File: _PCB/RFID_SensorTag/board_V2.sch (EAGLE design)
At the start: 21 parts, among them J2 SMT, J3 SMT, M2 BATTERY-CHARGER-LI-PROT, U1 MAXIM_ELECTRONICS_MAX40200AUK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, X1 53048-02

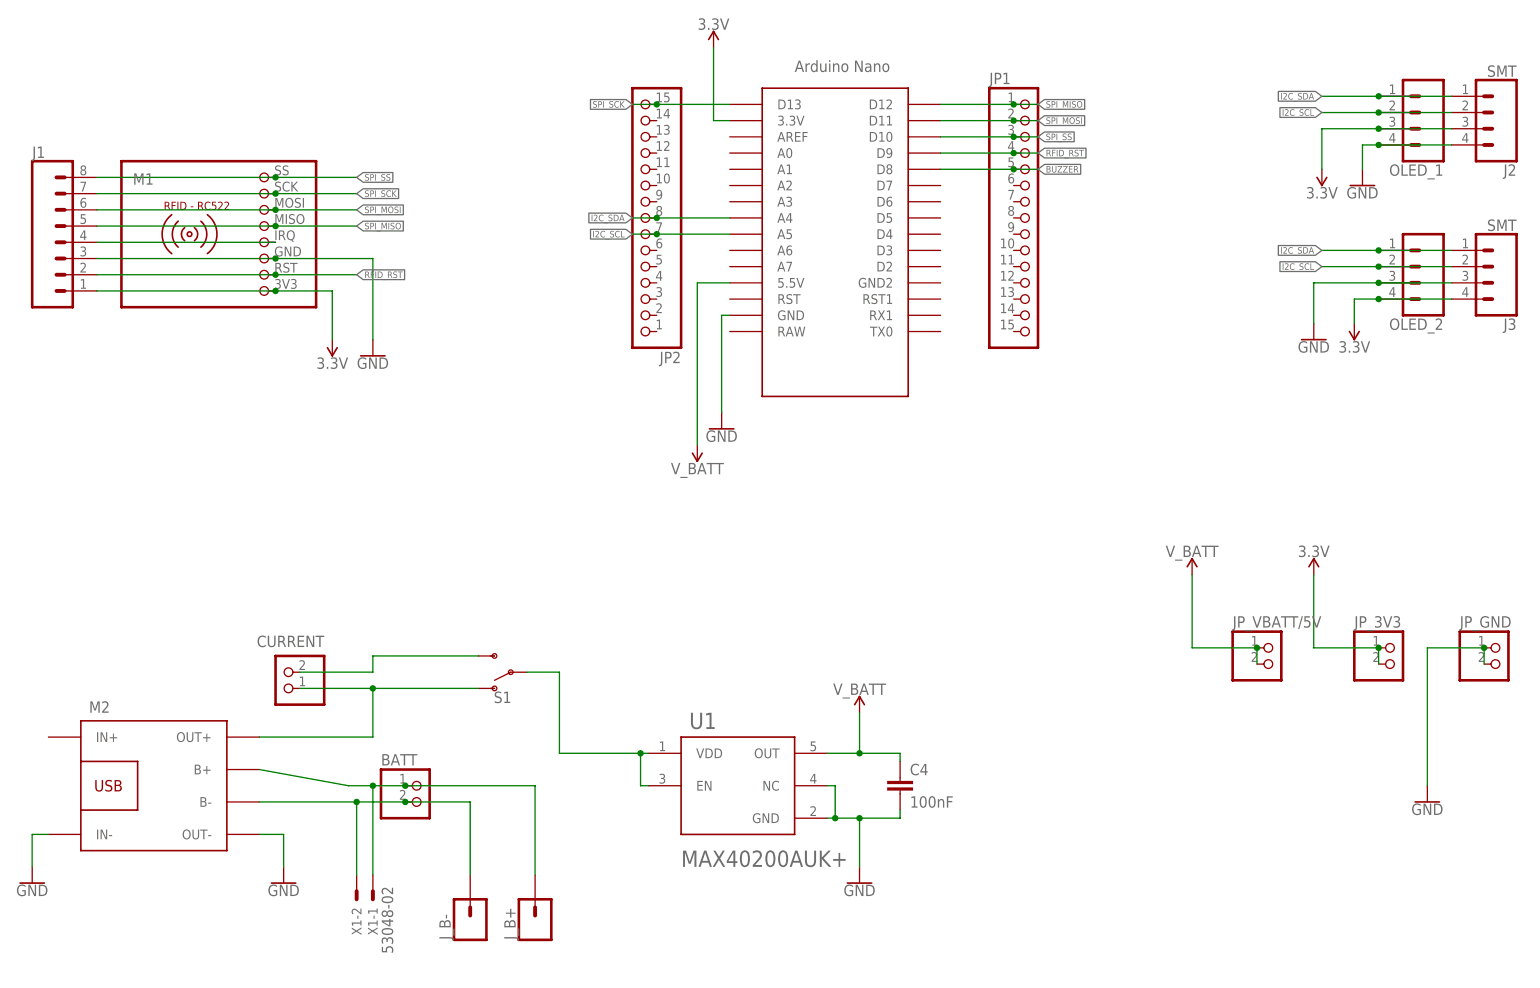
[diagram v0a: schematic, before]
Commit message: RFID system V2 out
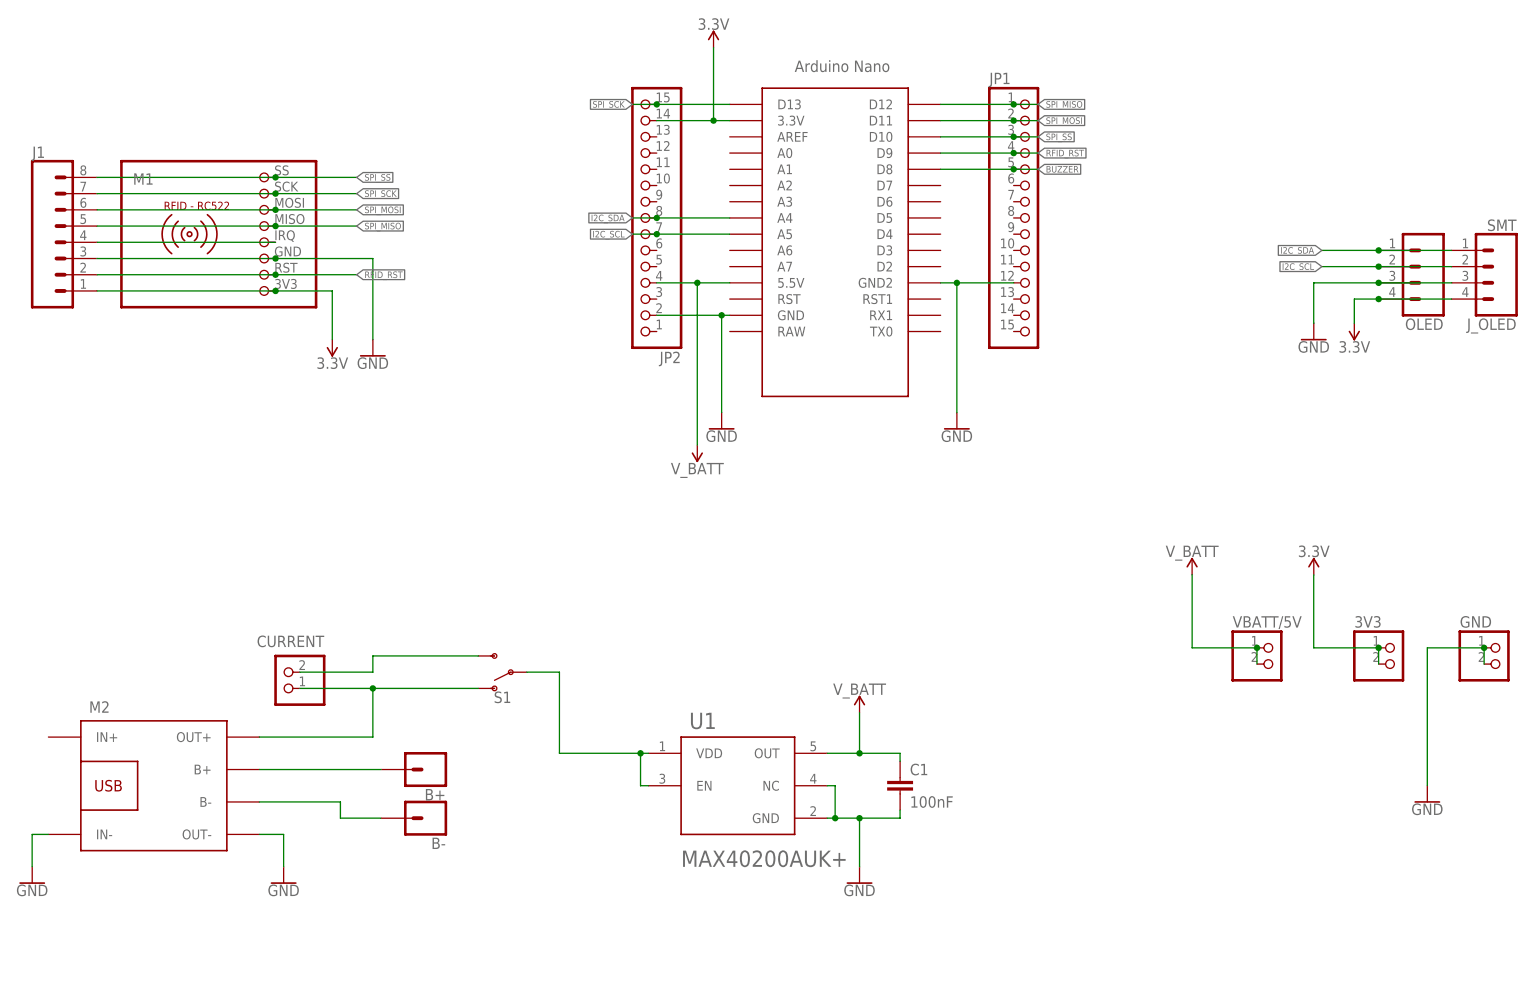
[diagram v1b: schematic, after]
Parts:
- removed BATT: (no value), pinhead:PINHD-1X2
- removed J2: SMT, SparkFun-Connectors:CONN_04SMD_STRAIGHT_COMBO
- removed J_B+, J_B-: (no value), SparkFun-Connectors:CONN_01OFFSET
- removed OLED_1: (no value), SparkFun-Connectors:CONN_04
- removed X1: 53048-02, con-molex:53048-02
- added B+, B-: (no value), SparkFun-Connectors:CONN_01OFFSET
- renumbered C4 to C1, J3 to J_OLED, JP_3V3 to 3V3, JP_GND to GND, JP_VBATT/5V to VBATT/5V, OLED_2 to OLED
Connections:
- net 3.3V: now also JP2.14; no longer J2.3, OLED_1.3
- net GND: now also JP1.12, JP2.2, U$1.GND2; no longer J2.4, OLED_1.4
- net I2C_SCL: no longer J2.2, OLED_1.2
- net I2C_SDA: no longer J2.1, OLED_1.1
- net N$1: now also B+.1; no longer BATT.1, J_B+.1, X1-1.S
- net N$5: now also B-.1; no longer BATT.2, J_B-.1, X1-2.S
- net V_BATT: now also JP2.4
